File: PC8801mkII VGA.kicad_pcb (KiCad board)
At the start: 2 copper layers, 39.4 x 31.8 mm, 8 parts

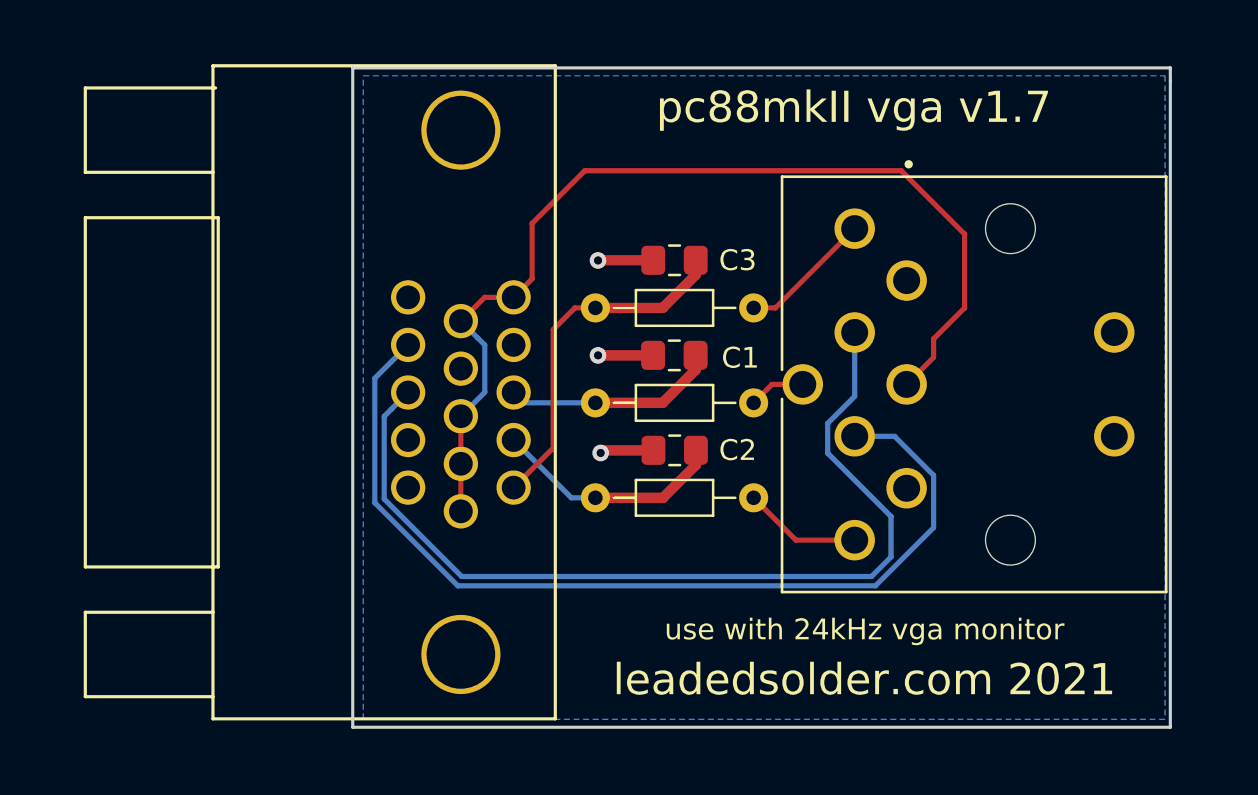
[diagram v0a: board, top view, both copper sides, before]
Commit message: KiCad 8; bring up to spec
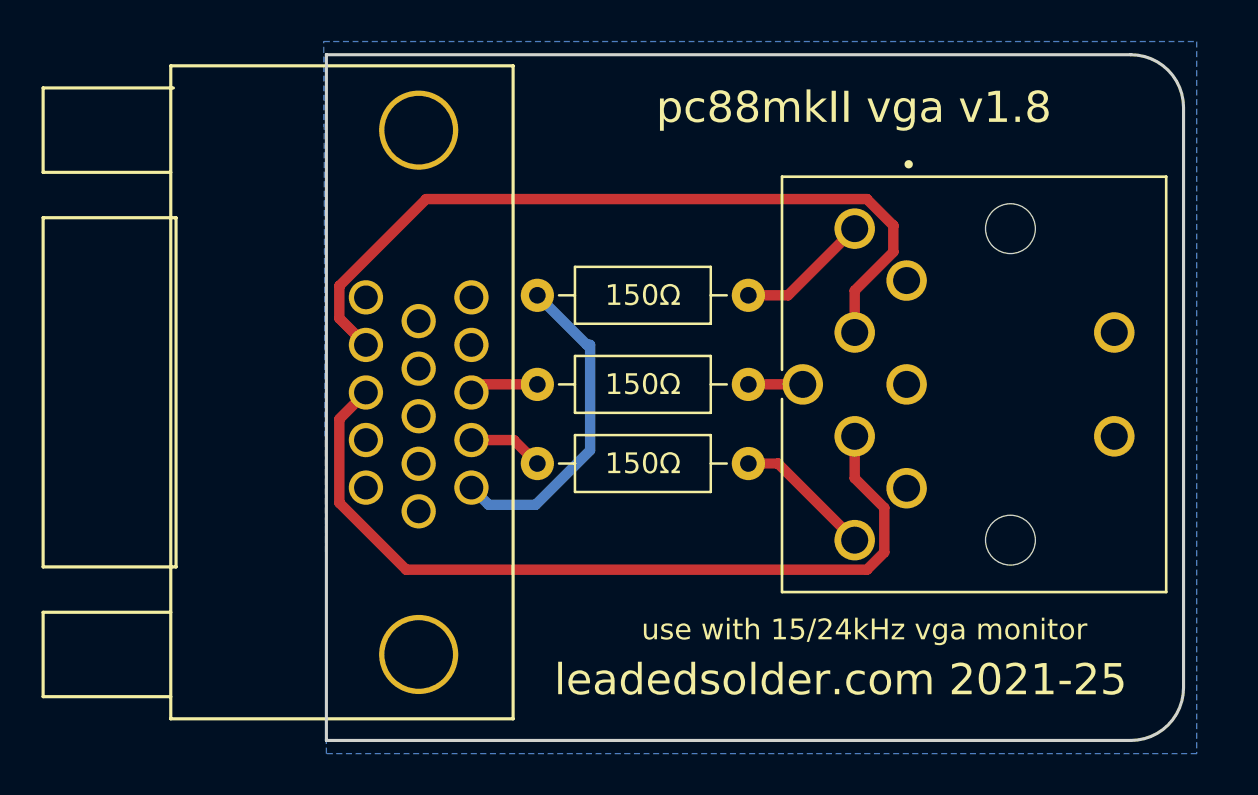
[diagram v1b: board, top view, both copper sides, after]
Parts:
- removed C1, C2, C3: 0.1µF, Capacitor_SMD:C_0805_2012Metric_Pad1.15x1.40mm_HandSolder
- removed RBlue1, RGreen1, RRed1: 150Ω, Resistors_ThroughHole:R_Axial_DIN0204_L3.6mm_D1.6mm_P7.62mm_Horizontal
- added R1: 150Ω, Resistor_THT:R_Axial_DIN0207_L6.3mm_D2.5mm_P10.16mm_Horizontal, F.Cu at (184.2, 103.0)
- added R2: 150Ω, Resistor_THT:R_Axial_DIN0207_L6.3mm_D2.5mm_P10.16mm_Horizontal, F.Cu at (184.2, 111.1)
- added R3: 150Ω, Resistor_THT:R_Axial_DIN0207_L6.3mm_D2.5mm_P10.16mm_Horizontal, F.Cu at (184.2, 107.3)
- moved V1 2.03 mm to (166.6, 107.7)
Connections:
- N1 pad 1: Net-(N1-Pad1) -> unconnected-(N1-Pad1)
- N1 pad 2: /GND -> GND
- N1 pad S1: (no net) -> GND
- N1 pad S2: (no net) -> GND
- V1 pad 10: /GND -> GND
- V1 pad 11: Net-(V1-Pad11) -> unconnected-(V1-P111-Pad11)
- V1 pad 12: Net-(V1-Pad12) -> unconnected-(V1-P12-Pad12)
- V1 pad 13: /V-Sync -> /H-Sync
- V1 pad 14: /H-Sync -> /V-Sync
- V1 pad 15: Net-(V1-Pad15) -> unconnected-(V1-P15-Pad15)
- V1 pad 16: (no net) -> GND
- V1 pad 17: (no net) -> GND
- V1 pad 4: Net-(V1-Pad4) -> unconnected-(V1-Pad4)
- V1 pad 5: /GND -> GND
- V1 pad 6: /GND -> GND
- V1 pad 7: /GND -> GND
- V1 pad 8: /GND -> GND
- V1 pad 9: /KEY -> unconnected-(V1-P9-Pad9)
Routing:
- net /GND: track 56.5 -> 0.00 mm, vias 3 -> 0
- net /Blue_VGA: track 11.3 -> 3.34 mm
- net /Green_VGA: track 11.3 -> 3.64 mm
- net /V-Sync: track 44.6 -> 38.2 mm
- net /H-Sync: track 45.1 -> 39.9 mm
- net /Red_VGA: track 17.1 -> 15.7 mm
- net /Green: track 5.88 -> 6.65 mm
- added copper zone on B.Cu, net GND
- removed copper zone on B.Cu, net /GND
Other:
- board size 39.4 x 31.8 mm -> 41.3 x 33 mm
- net class Default removed
- board text added: "b"
- board text added: "g"
- board text added: "hs"
- board text added: "leadedsolder.com 2021-25"
- board text added: "pc88mkII vga v1.8"
- board text added: "r"
- board text added: "use with 15/24kHz vga monitor"
- board text added: "vs"
- board text removed: "150Ω resistors"
- board text removed: "Blue"
- board text removed: "Green"
- board text removed: "Red"
- board text removed: "leadedsolder.com 2021"
- board text removed: "pc88mkII vga v1.7"
- board text removed: "use with 24kHz vga monitor"

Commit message: v1.9 test release
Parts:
- added C1: 0.1µF, Capacitor_THT:C_Disc_D3.4mm_W2.1mm_P2.50mm, F.Cu at (186.7, 103.5)
- added C2: 0.1µF, Capacitor_THT:C_Disc_D3.4mm_W2.1mm_P2.50mm, F.Cu at (186.7, 118.1)
- added C3: 0.1µF, Capacitor_THT:C_Disc_D3.4mm_W2.1mm_P2.50mm, F.Cu at (186.7, 110.5)
- moved R2 3.17 mm to (184.2, 114.3)
- moved R1 2.70 mm to (184.2, 100.3)
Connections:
- R1 pad 1: /Red_VGA -> Net-(C1-Pad1)
- R2 pad 1: /Green_VGA -> Net-(C2-Pad1)
- R3 pad 1: /Blue_VGA -> Net-(C3-Pad1)
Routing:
- net /Green_VGA: track 3.64 -> 10.5 mm
- net Net-(C2-Pad1): track 0.00 -> 4.86 mm
- net Net-(C3-Pad1): track 0.00 -> 4.22 mm
- net Net-(C1-Pad1): track 0.00 -> 4.21 mm
- net /H-Sync: track 39.9 -> 42.5 mm
- net /Green: track 6.65 -> 5.33 mm
- net /Red: track 6.45 -> 5.33 mm
- net /Blue_VGA: track 3.34 -> 4.35 mm
- net /Red_VGA: track 15.7 -> 16.6 mm
